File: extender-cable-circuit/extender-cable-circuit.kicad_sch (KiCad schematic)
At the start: 37 parts, among them X3 24MHz

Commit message: Working on rally compact layout for cable extender.
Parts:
- removed C3: 100nF, Library:C0402, symbol Library:CC0402KRX7R7BB104 Capacitor 100nF
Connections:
- net 3V3A is gone; now on net 3V3: C10.2, C12.2, C13.2, C5.2, C7.2, L2.2, U1.10 (VDDA33), U1.29 (VDDA33), U1.36 (VDDA33), U1.5 (VDDA33)
- net 5V is gone; now on net VBUS: C20.2, U3.1 (IN), U3.3 (EN)
- net 3V3: no longer C8.2, L2.1, U3.5 (OUT)
- new net 3V3-before-filter: C8.2, L2.1, U3.5 (OUT)
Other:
- sheet servo-usb-connector ports: added VBUS; removed 5V
- sheet servo-usb-connector1 ports: added VBUS; removed 5V
- sheet servo-usb-connector2 ports: added VBUS; removed 5V
- sheet servo-usb-connector3 ports: added VBUS; removed 5V
- moved on the sheet: R54

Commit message: Work on cable outline, and almost finish wiring.
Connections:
- net GND: now also FPC0.11, FPC0.12, FPC0.13, FPC0.14, FPC0.15, FPC0.16, FPC0.17, FPC0.18, FPC0.19, FPC0.20; no longer FPC0.1, FPC0.10, FPC0.2, FPC0.3, FPC0.4, FPC0.5, FPC0.6, FPC0.7, FPC0.8, FPC0.9
- net VCC: now also FPC0.1, FPC0.10, FPC0.2, FPC0.3, FPC0.4, FPC0.5, FPC0.6, FPC0.7, FPC0.8, FPC0.9; no longer FPC0.11, FPC0.12, FPC0.13, FPC0.14, FPC0.15, FPC0.16, FPC0.17, FPC0.18, FPC0.19, FPC0.20

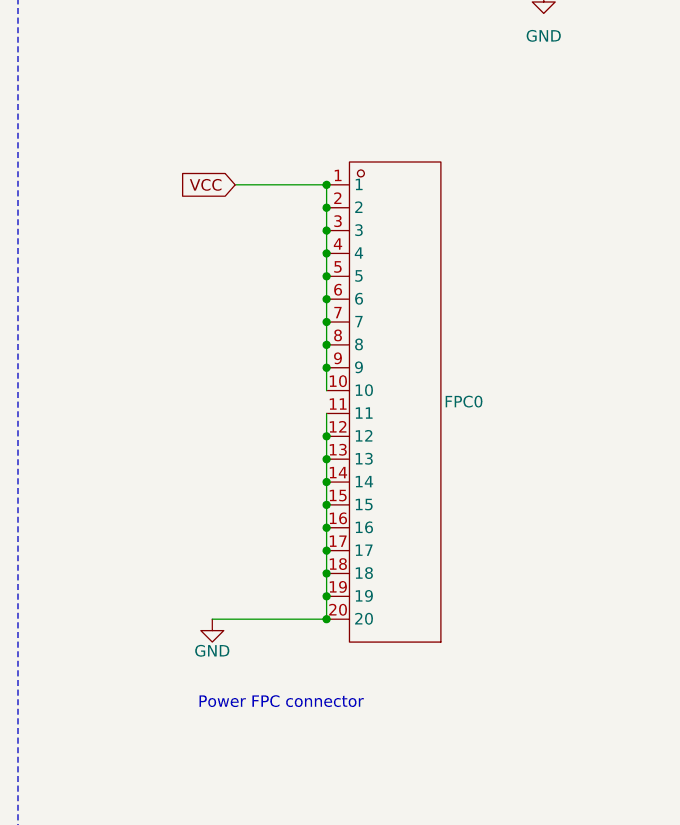
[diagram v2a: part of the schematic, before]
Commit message: Finish extender cable circuit.
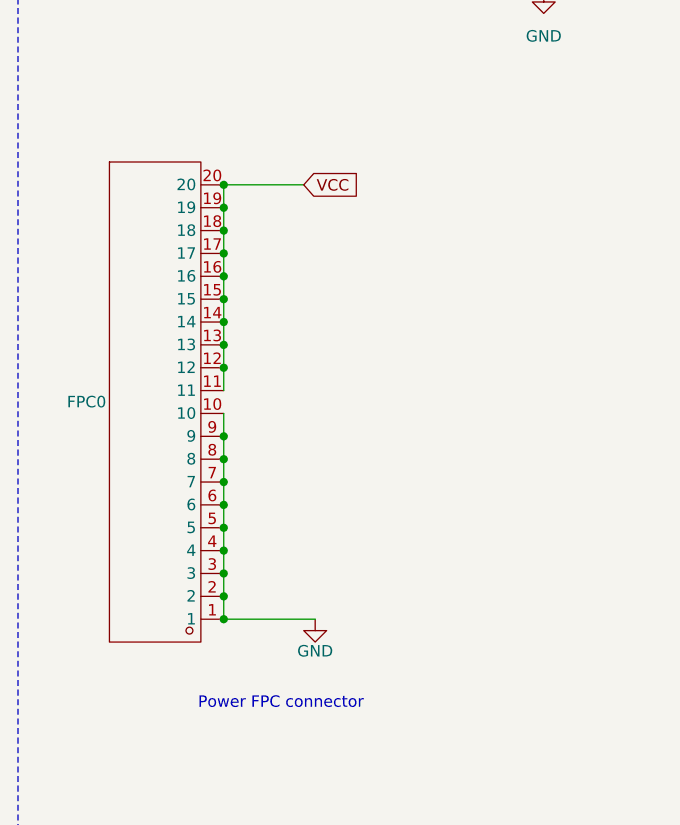
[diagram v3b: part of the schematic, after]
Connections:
- net GND: now also FPC0.1, FPC0.10, FPC0.2, FPC0.3, FPC0.4, FPC0.5, FPC0.6, FPC0.7, FPC0.8, FPC0.9; no longer FPC0.11, FPC0.12, FPC0.13, FPC0.14, FPC0.15, FPC0.16, FPC0.17, FPC0.18, FPC0.19, FPC0.20
- net VCC: now also FPC0.11, FPC0.12, FPC0.13, FPC0.14, FPC0.15, FPC0.16, FPC0.17, FPC0.18, FPC0.19, FPC0.20; no longer FPC0.1, FPC0.10, FPC0.2, FPC0.3, FPC0.4, FPC0.5, FPC0.6, FPC0.7, FPC0.8, FPC0.9
